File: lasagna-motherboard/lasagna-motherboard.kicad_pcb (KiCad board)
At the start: 2 copper layers, 230.4 x 97.8 mm, 16 parts, among them J1 Jetson_Power_Connector, J2 Fathom_X_Connector, J3 Power_Connector, U1 Adafruit_BNO055_IMU, U10 ESC, U11 ESC, U12 ESC, U13 ESC, U2 Jetson_Xavier_NX_Mounting_Hol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, U3 Jetson_Xavier_NX_Pins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

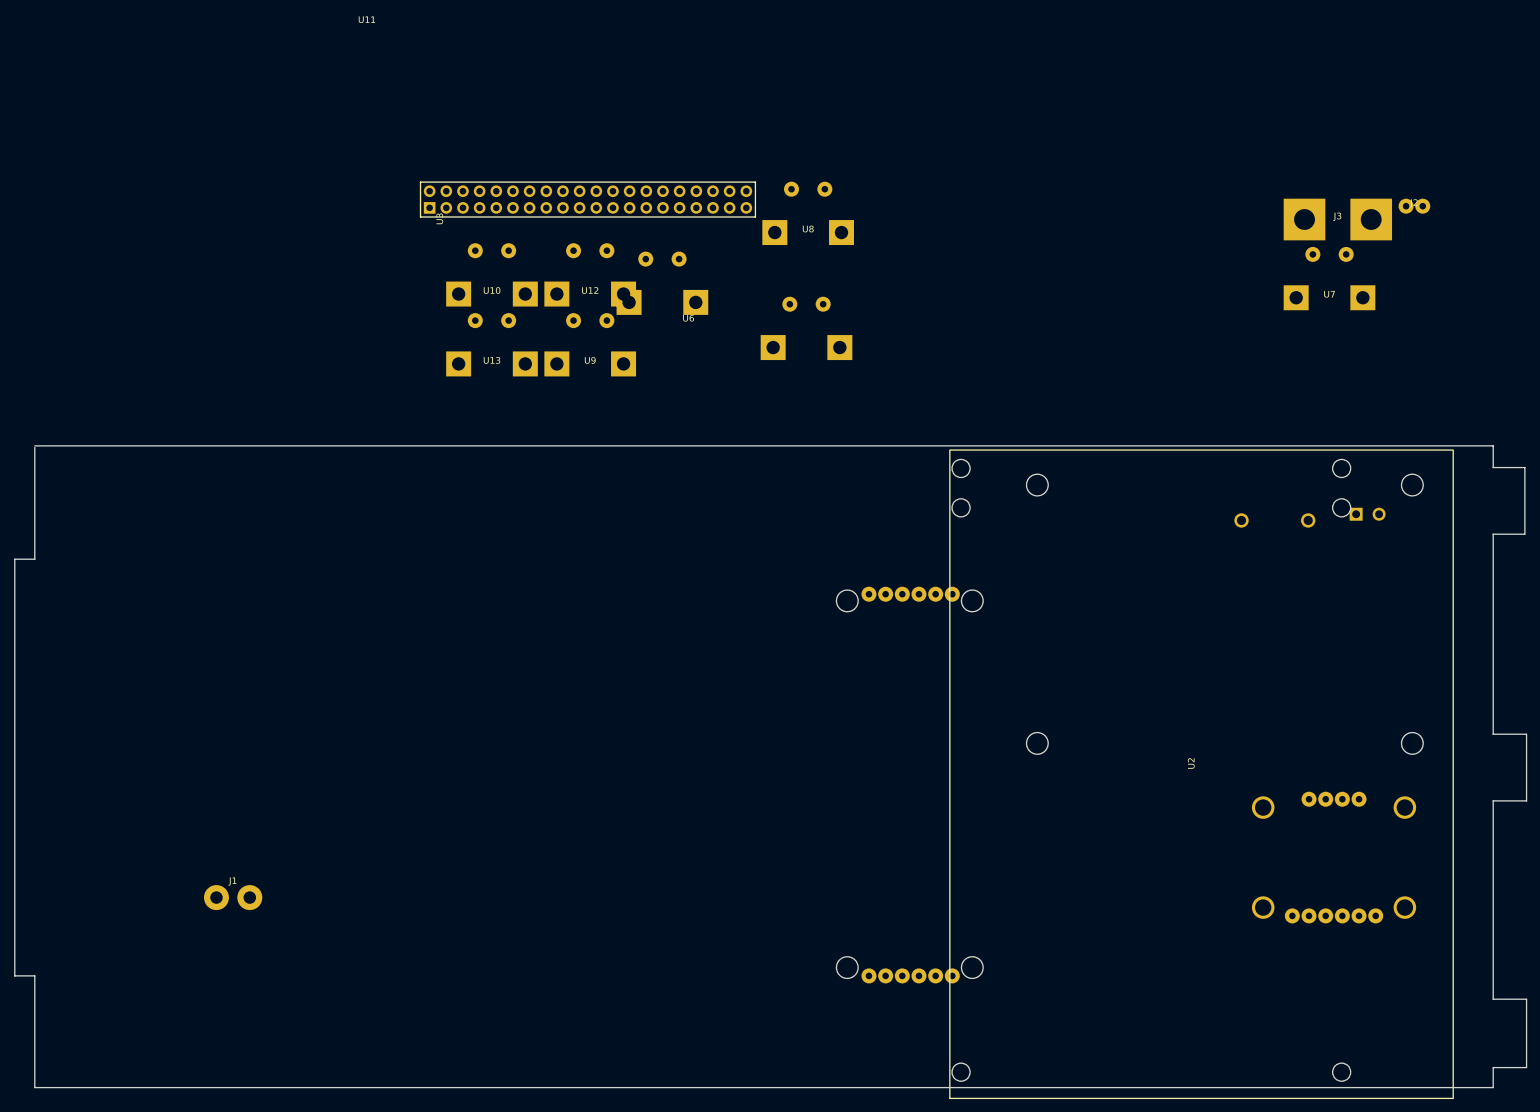
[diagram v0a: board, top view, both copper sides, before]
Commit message: added the servo connectors
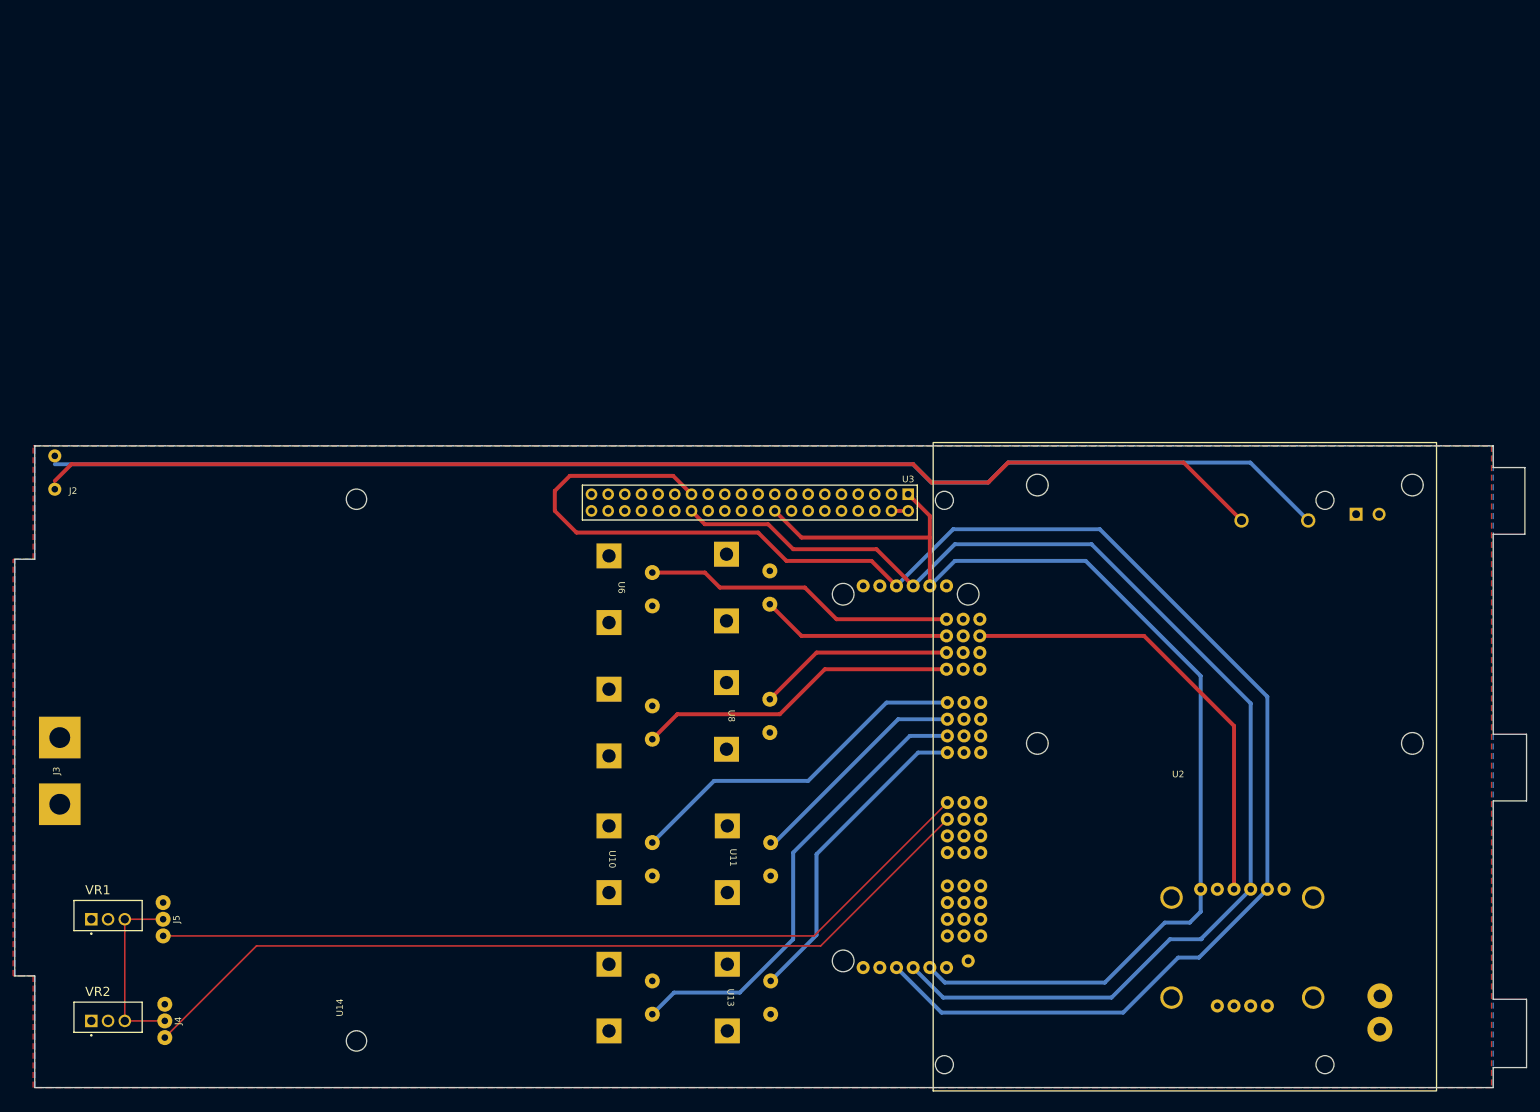
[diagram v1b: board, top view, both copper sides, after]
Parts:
- added J4: Servo_Connector, lasagna-motherboard:Servo PWM Connector, F.Cu at (60.7, 150.9)
- added J5: Servo_Connector, lasagna-motherboard:Servo PWM Connector, F.Cu at (60.5, 135.4)
- added U14: ESC_Holder_Mounting_Holes, lasagna-motherboard:ESC Holder mounting Holes, F.Cu at (87.4, 153.9)
- added VR1: 7805_TO-220_Voltage_Regulator, lasagna-motherboard:Voltage Regulator TO255, F.Cu at (47.0, 135.4)
- added VR2: 7805_TO-220_Voltage_Regulator, lasagna-motherboard:Voltage Regulator TO255, F.Cu at (47.0, 150.9)
- J1, U12, U7, U9: moved to B.Cu
- moved J3 212.1 mm to (42.2, 112.8), turned to 90 degrees
- moved J2 211.1 mm to (41.4, 67.3), turned to 90 degrees
- moved J1 175.6 mm to (243.3, 149.6), turned to -90 degrees
- moved U12 107.3 mm to (125.9, 147.3), turned to 90 degrees
- moved U13 103.0 mm to (143.9, 147.3), turned to -90 degrees
- moved U7 102.0 mm to (143.8, 84.8), turned to 90 degrees
- moved U10 88.0 mm to (125.9, 126.2), turned to -90 degrees
- moved U11 78.9 mm to (143.9, 126.2), turned to -90 degrees
- moved U8 74.7 mm to (143.8, 104.4), turned to -90 degrees
- moved U9 54.7 mm to (125.9, 105.4), turned to 90 degrees
- moved U3 52.4 mm to (147.3, 71.9), turned to 180 degrees
- moved U6 44.5 mm to (125.9, 85.1), turned to -90 degrees
- moved U5 35.6 mm to (183.9, 82.5), turned to -90 degrees
- moved U1 20.5 mm to (221.7, 139.7), turned to 0 degrees
- moved U2 2.79 mm to (212.1, 110.5)
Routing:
- net Net-(U1-Pad9): track 0.00 -> 249.9 mm
- net Net-(J2-Pad2): track 0.00 -> 197.1 mm
- net Net-(U1-Pad8): track 0.00 -> 191.2 mm
- net Net-(J2-Pad1): track 0.00 -> 188.0 mm
- net +3V3: track 0.00 -> 173.4 mm
- net Net-(U5-Pad40): track 0.00 -> 133.0 mm
- net Net-(U5-Pad37): track 0.00 -> 127.9 mm
- net Net-(U12-Pad3): track 0.00 -> 70.3 mm
- net GND: track 0.00 -> 69.3 mm
- net Net-(U10-Pad3): track 0.00 -> 53.8 mm
- net Net-(U5-Pad22): track 0.00 -> 49.2 mm
- net Net-(U13-Pad3): track 0.00 -> 48.6 mm
- net Net-(U5-Pad13): track 0.00 -> 47.8 mm
- net Net-(U11-Pad3): track 0.00 -> 34.7 mm
- net Net-(U5-Pad19): track 0.00 -> 29.9 mm
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- added copper zone on F.Cu, net +12V
- added copper zone on B.Cu, net GND
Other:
- outline, holes or cut-outs redrawn
